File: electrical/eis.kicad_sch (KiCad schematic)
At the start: 57 parts

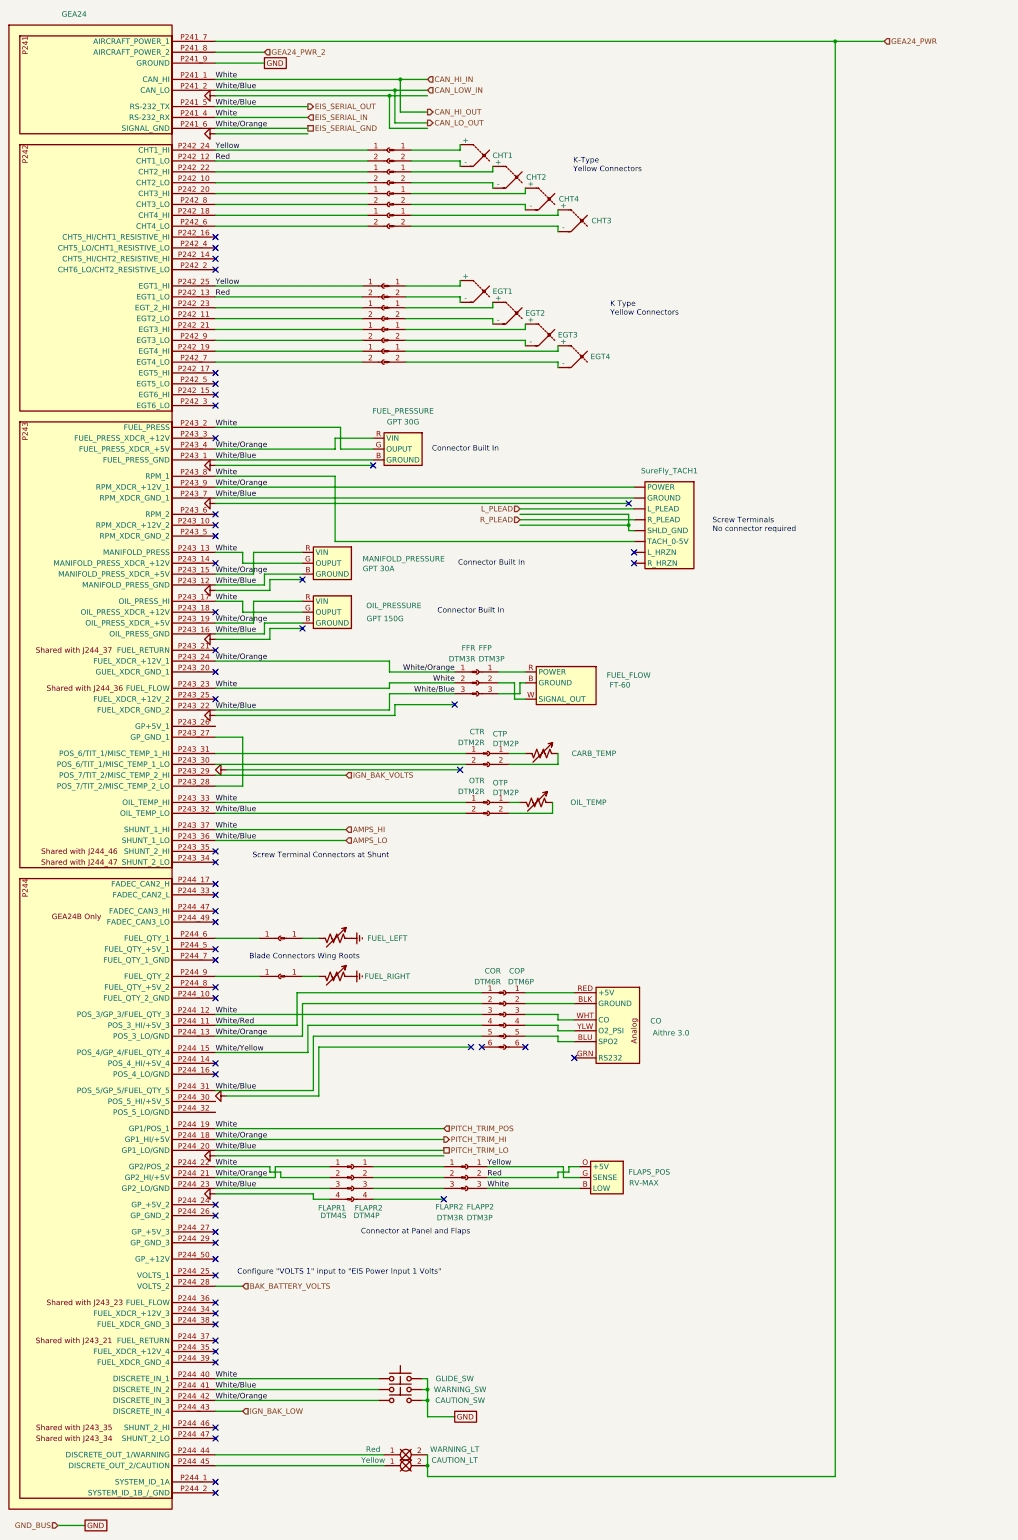
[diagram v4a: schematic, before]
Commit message: Assumed engine connector is sufficient for wiring on bench..
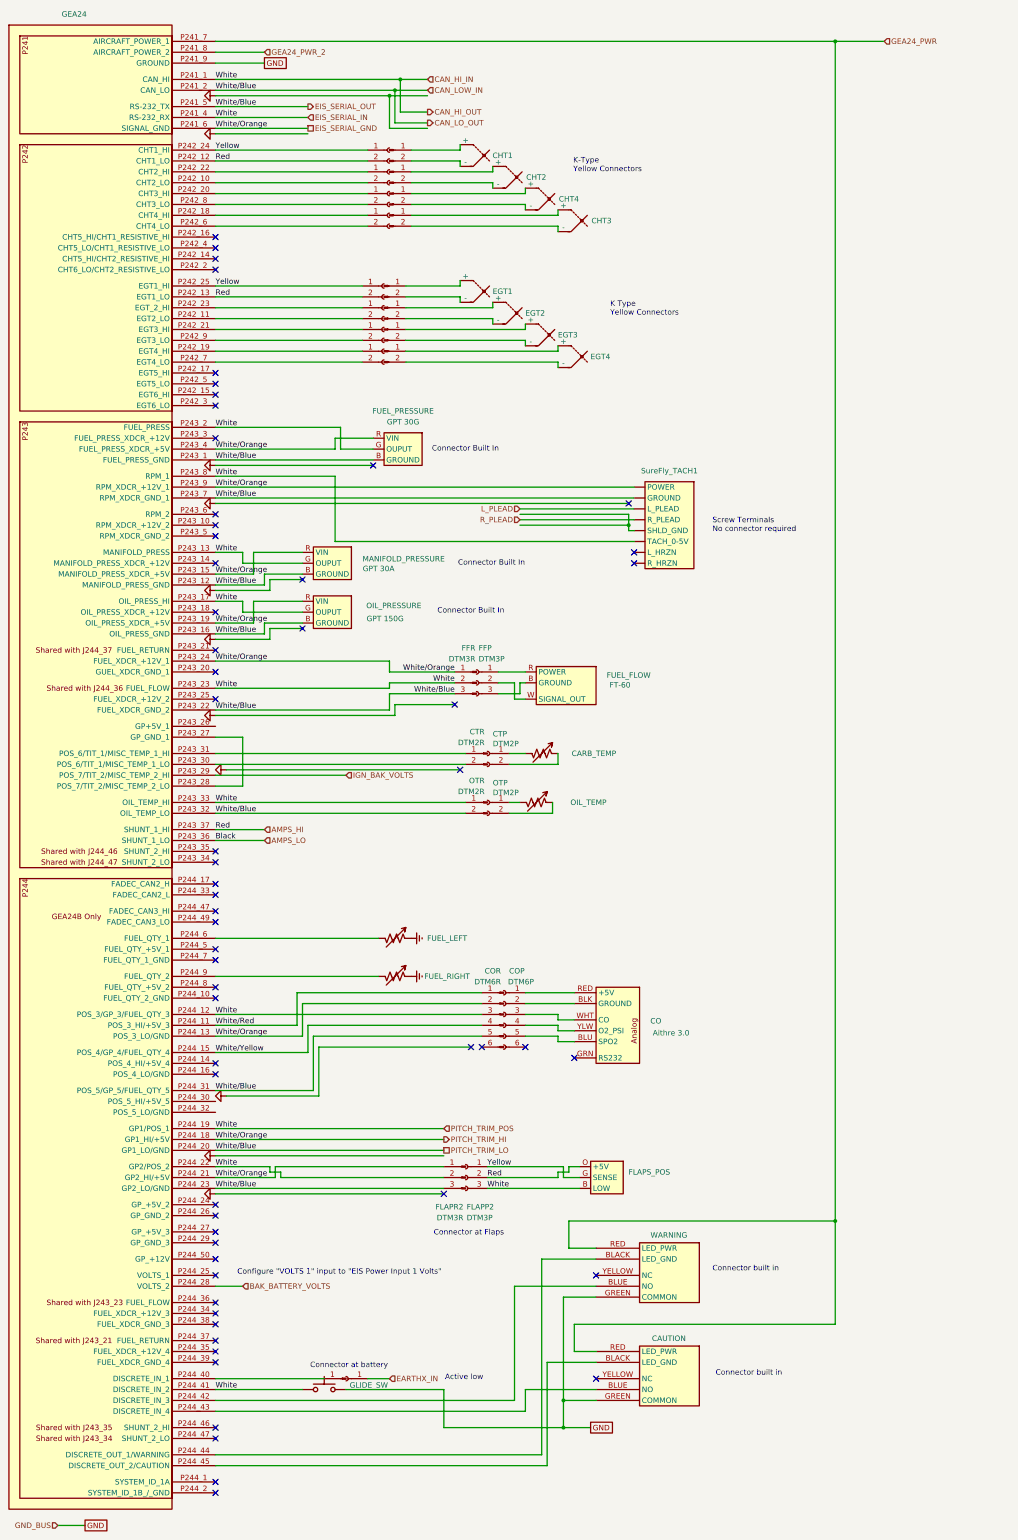
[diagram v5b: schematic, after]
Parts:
- removed CAUTION_LT: Yellow, symbol FlyerX:Bulb
- removed CAUTION_SW, WARNING_SW: SW_Push, symbol Switch:SW_Push
- removed FLAPR1: DTM4S, symbol Connector:Conn_01x04_Pin
- removed FLAPR2: DTM4P, symbol Connector:Conn_01x04_Socket
- removed LFP, RFP: Conn_01x01_Pin, symbol Connector:Conn_01x01_Pin
- removed LFR, RFR: Conn_01x01_Socket, symbol Connector:Conn_01x01_Socket
- removed WARNING_LT: Red, symbol FlyerX:Bulb
- added CAUTION, WARNING: ~, symbol flyerx:Apiele_Momentary_Illuminated_Button
- added EARTHXP: Conn_01x01_Pin, symbol Connector:Conn_01x01_Pin
- added EARTHXS: Conn_01x01_Socket, symbol Connector:Conn_01x01_Socket
- FLAPS_POS: value RV-MAX -> ~
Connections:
- net Red is gone; now on net AMPS_HI: CHT1R.2 (Pin_2), EGT1R.2 (Pin_2), FLAPP2.2 (Pin_2), FLAPS_POS.O (+5V), GEA24.P242_12 (CHT1_LO), GEA24.P242_13 (EGT1_LO)
- net AMPS_HI: no longer COR.3 (Pin_3), FFR.2 (Pin_2), FLAPP2.3 (Pin_3), FLAPS_POS.B (LOW), FUEL_PRESSURE.G (OUPUT), GEA24.P241_1 (CAN_HI), GEA24.P241_4 (RS-232_RX), GEA24.P243_13 (MANIFOLD_PRESS), GEA24.P243_17 (OIL_PRESS_HI), GEA24.P243_2 (FUEL_PRESS), GEA24.P243_23 (FUEL_FLOW), GEA24.P243_33 (OIL_TEMP_HI), GEA24.P243_8 (RPM_1), GEA24.P244_12 (POS_3/GP_3/FUEL_QTY_3), GEA24.P244_19 (GP1/POS_1), GEA24.P244_22 (GP2/POS_2), GEA24.P244_40 (DISCRETE_IN_1), GLIDE_SW.1, MANIFOLD_PRESSURE.G (OUPUT), OIL_PRESSURE.G (OUPUT), OTR.1 (Pin_1), SureFly_TACH1. (R_HRZN)
- net AMPS_LO: no longer COR.5 (Pin_5), FFR.3 (Pin_3), FUEL_PRESSURE.B (GROUND), GEA24.P241_2 (CAN_LO), GEA24.P241_5 (RS-232_TX), GEA24.P243_1 (FUEL_PRESS_GND), GEA24.P243_12 (MANIFOLD_PRESS_GND), GEA24.P243_16 (OIL_PRESS_GND), GEA24.P243_22 (FUEL_XDCR_GND_2), GEA24.P243_32 (OIL_TEMP_LO), GEA24.P243_7 (RPM_XDCR_GND_1), GEA24.P244_20 (GP1_LO/GND), GEA24.P244_23 (GP2_LO/GND), GEA24.P244_31 (POS_5/GP_5/FUEL_QTY_5), GEA24.P244_41 (DISCRETE_IN_2), MANIFOLD_PRESSURE.B (GROUND), OIL_PRESSURE.B (GROUND), OTR.2 (Pin_2), SureFly_TACH1. (R_HRZN)
- net EIS_SERIAL_GND: now also FLAPR2.1 (Pin_1); no longer GEA24.P244_42 (DISCRETE_IN_3)
- net GEA24_PWR: now also CAUTION.RED (LED_PWR), WARNING.RED (LED_PWR)
- net GND: now also CAUTION.GREEN (COMMON), WARNING.GREEN (COMMON)
- net at GEA24.P244_6 (FUEL_QTY_1): now also FUEL_LEFT.2
- net CAN_HI_IN: now reaches FLAPR2.2 (Pin_2)
- net CAN_HI_IN: now also COR.3 (Pin_3), FFR.2 (Pin_2), FLAPP2.3 (Pin_3), FLAPS_POS.B (LOW), FUEL_PRESSURE.G (OUPUT), GEA24.P241_1 (CAN_HI), GEA24.P241_4 (RS-232_RX), GEA24.P243_13 (MANIFOLD_PRESS), GEA24.P243_17 (OIL_PRESS_HI), GEA24.P243_2 (FUEL_PRESS), GEA24.P243_23 (FUEL_FLOW), GEA24.P243_33 (OIL_TEMP_HI), GEA24.P243_8 (RPM_1), GEA24.P244_12 (POS_3/GP_3/FUEL_QTY_3), GEA24.P244_19 (GP1/POS_1), GEA24.P244_22 (GP2/POS_2), GEA24.P244_41 (DISCRETE_IN_2), GLIDE_SW.1, MANIFOLD_PRESSURE.G (OUPUT), OIL_PRESSURE.G (OUPUT), OTR.1 (Pin_1), SureFly_TACH1. (R_HRZN)
- net CAN_LOW_IN: now reaches FLAPR2.3 (Pin_3)
- net CAN_LOW_IN: now also COR.5 (Pin_5), FFR.3 (Pin_3), FUEL_PRESSURE.B (GROUND), GEA24.P241_2 (CAN_LO), GEA24.P241_5 (RS-232_TX), GEA24.P243_1 (FUEL_PRESS_GND), GEA24.P243_12 (MANIFOLD_PRESS_GND), GEA24.P243_16 (OIL_PRESS_GND), GEA24.P243_22 (FUEL_XDCR_GND_2), GEA24.P243_32 (OIL_TEMP_LO), GEA24.P243_7 (RPM_XDCR_GND_1), GEA24.P244_20 (GP1_LO/GND), GEA24.P244_23 (GP2_LO/GND), GEA24.P244_31 (POS_5/GP_5/FUEL_QTY_5), MANIFOLD_PRESSURE.B (GROUND), OIL_PRESSURE.B (GROUND), OTR.2 (Pin_2), SureFly_TACH1. (R_HRZN)
- net at GEA24.P244_44 (DISCRETE_OUT_1/WARNING): now also WARNING.BLACK (LED_GND)
- net at GEA24.P244_45 (DISCRETE_OUT_2/CAUTION): now also CAUTION.BLACK (LED_GND)
- net at GEA24.P244_9 (FUEL_QTY_2): now also FUEL_RIGHT.2
- net IGN_BAK_LOW: no longer names the net of GEA24.P244_43 (DISCRETE_IN_4)
- net IGN_BAK_LOW: now also CAUTION.BLUE (NO)
- new net: EARTHXP.1 (Pin_1), GEA24.P244_40 (DISCRETE_IN_1)
- new net: GEA24.P244_42 (DISCRETE_IN_3), WARNING.BLUE (NO)
- new net EARTHX_IN: EARTHXS.1 (Pin_1)
- no-connect marks 58 -> 60
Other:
- note added: "Active low"
- note added: "Connector at Flaps"
- note added: "Connector at battery"
- note added: "Connector built in"
- note removed: "Blade Connectors Wing Roots"
- note removed: "Connector at Panel and Flaps"
- note removed: "Screw Terminal Connectors at Shunt"
- moved on the sheet: FUEL_LEFT, FUEL_RIGHT, GLIDE_SW

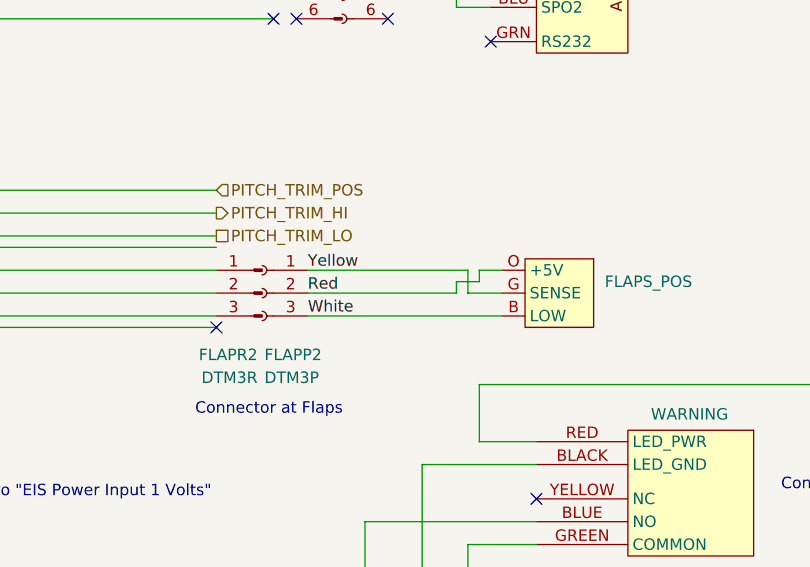
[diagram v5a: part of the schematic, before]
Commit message: Made flaps position sensor match colors of POS-12.
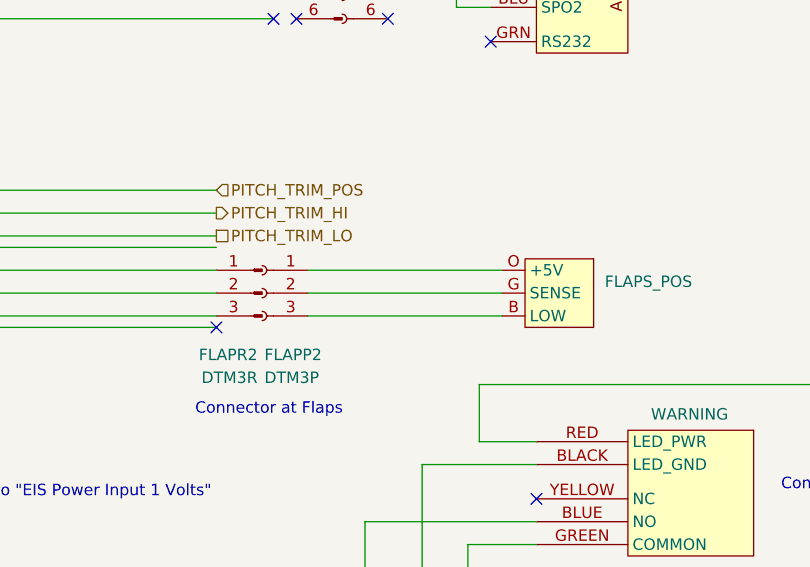
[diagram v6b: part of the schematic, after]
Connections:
- net AMPS_HI: no longer FLAPP2.2 (Pin_2), FLAPS_POS.O (+5V)
- net CAN_HI_IN: no longer FLAPP2.3 (Pin_3), FLAPS_POS.B (LOW)
- net Yellow: no longer FLAPP2.1 (Pin_1), FLAPS_POS.G (SENSE)
- new net: FLAPP2.1 (Pin_1), FLAPS_POS.O (+5V)
- new net: FLAPP2.2 (Pin_2), FLAPS_POS.G (SENSE)
- new net: FLAPP2.3 (Pin_3), FLAPS_POS.B (LOW)
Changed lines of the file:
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@@
 	(title_block
 		(title "EIS")
-		(date "2026-01-03")
-		(rev "1.2.4")
+		(date "2026-01-05")
+		(rev "1.2.5")
 		(company "N877RV")
 	)
@@
 	(wire
 		(pts
-			(xy 148.59 287.02) (xy 152.4 287.02)
-		)
-		(stroke
-			(width 0)
-			(type default)
-		)
-	)
-	(wire
-		(pts
 			(xy 86.36 243.84) (xy 129.54 243.84)
 		)
@@
 	(wire
 		(pts
-			(xy 148.59 284.48) (xy 148.59 287.02)
-		)
-		(stroke
-			(width 0)
-			(type default)
-		)
-	)
-	(wire
-		(pts
 			(xy 109.22 33.02) (xy 116.84 33.02)
 		)
@@
 	(wire
 		(pts
-			(xy 147.32 285.75) (xy 149.86 285.75)
-		)
-		(stroke
-			(width 0)
-			(type default)
-		)
-	)
-	(wire
-		(pts
 			(xy 67.31 193.04) (xy 97.79 193.04)
 		)
@@
 	(wire
 		(pts
-			(xy 130.81 284.48) (xy 148.59 284.48)
+			(xy 130.81 284.48) (xy 152.4 284.48)
 		)
 		(stroke
@@
 	(wire
 		(pts
-			(xy 147.32 287.02) (xy 147.32 285.75)
-		)
-		(stroke
-			(width 0)
-			(type default)
-		)
-	)
-	(wire
-		(pts
 			(xy 67.31 59.69) (xy 102.87 59.69)
 		)
@@
 	(wire
 		(pts
-			(xy 149.86 284.48) (xy 152.4 284.48)
-		)
-		(stroke
-			(width 0)
-			(type default)
-		)
-	)
-	(wire
-		(pts
 			(xy 139.7 341.63) (xy 139.7 336.55)
 		)
@@
 	(wire
 		(pts
-			(xy 130.81 287.02) (xy 147.32 287.02)
+			(xy 130.81 287.02) (xy 152.4 287.02)
 		)
 		(stroke
@@
 		(pts
 			(xy 67.31 26.67) (xy 78.74 26.67)
-		)
-		(stroke
-			(width 0)
-			(type default)
-		)
-	)
-	(wire
-		(pts
-			(xy 149.86 285.75) (xy 149.86 284.48)
 		)
 		(stroke
@@
 		)
 	)
-	(label "Red"
-		(at 130.81 287.02 0)
-		(effects
-			(font
-				(size 1.27 1.27)
-			)
-			(justify left bottom)
-		)
-	)
 	(label "White{slash}Blue"
 		(at 67.31 36.83 0)
@@
 		)
 	)
-	(label "White"
-		(at 130.81 289.56 0)
-		(effects
-			(font
-				(size 1.27 1.27)
-			)
-			(justify left bottom)
-		)
-	)
 	(label "White{slash}Orange"
 		(at 67.31 166.37 0)
@@
 		(effects
 			(font
-				(size 1.27 1.27)
-			)
-			(justify left bottom)
-		)
-	)
-	(label "Yellow"
-		(at 130.81 284.48 0)
-		(effects
-			(font

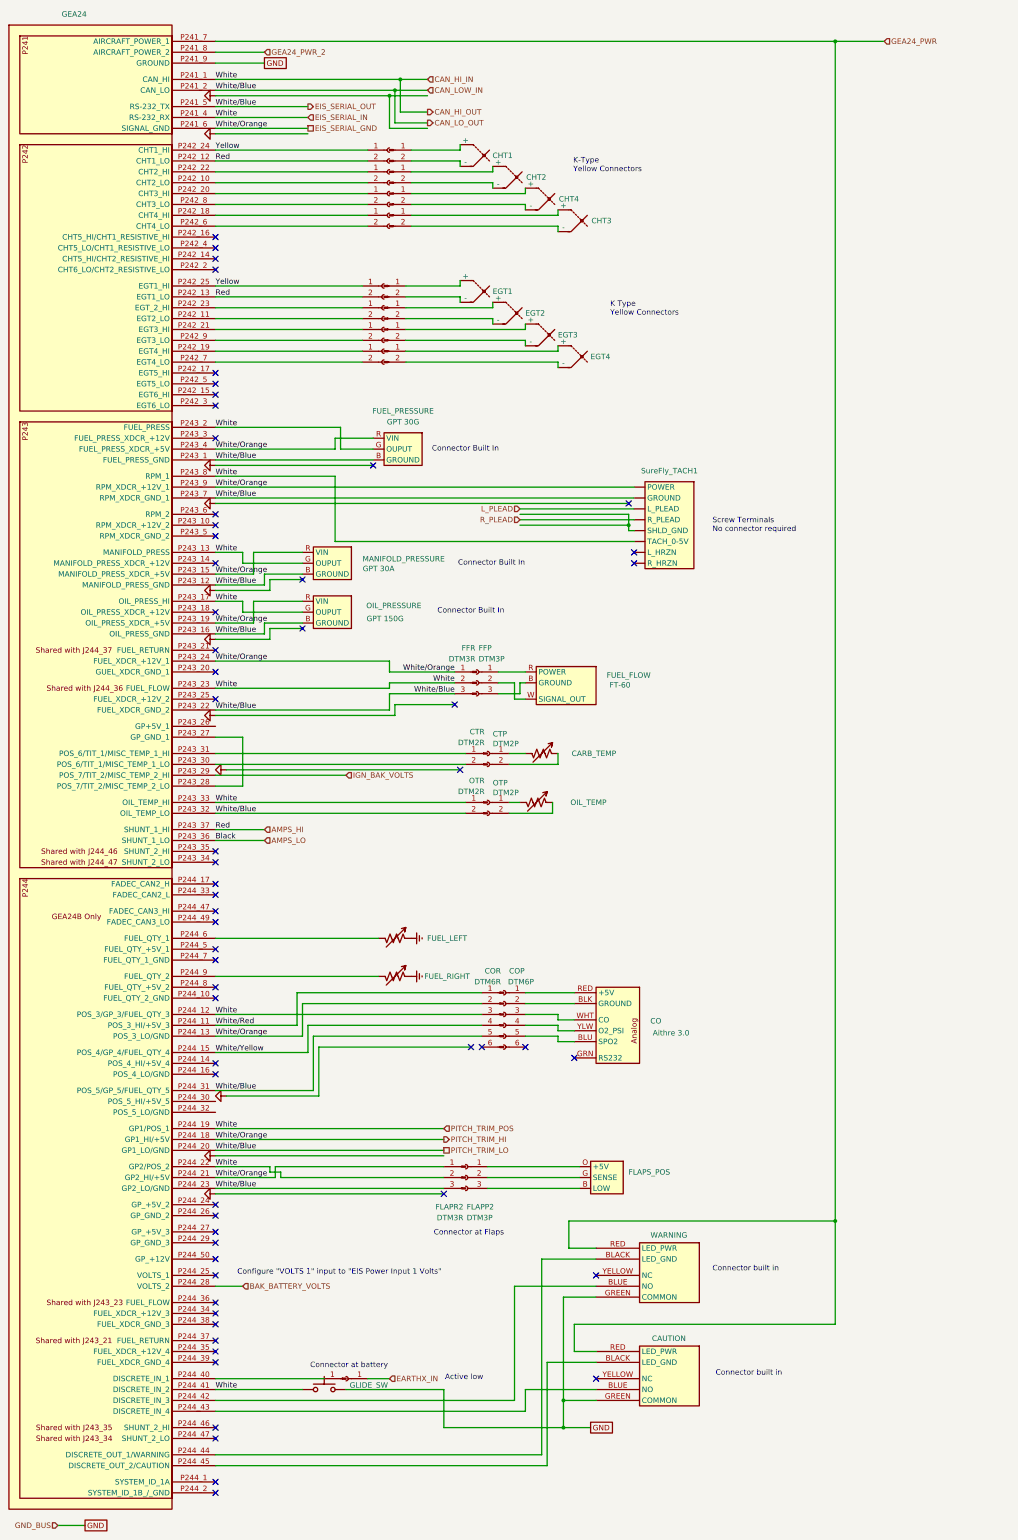
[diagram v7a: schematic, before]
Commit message: Added connector for discrete buttons on EIS.
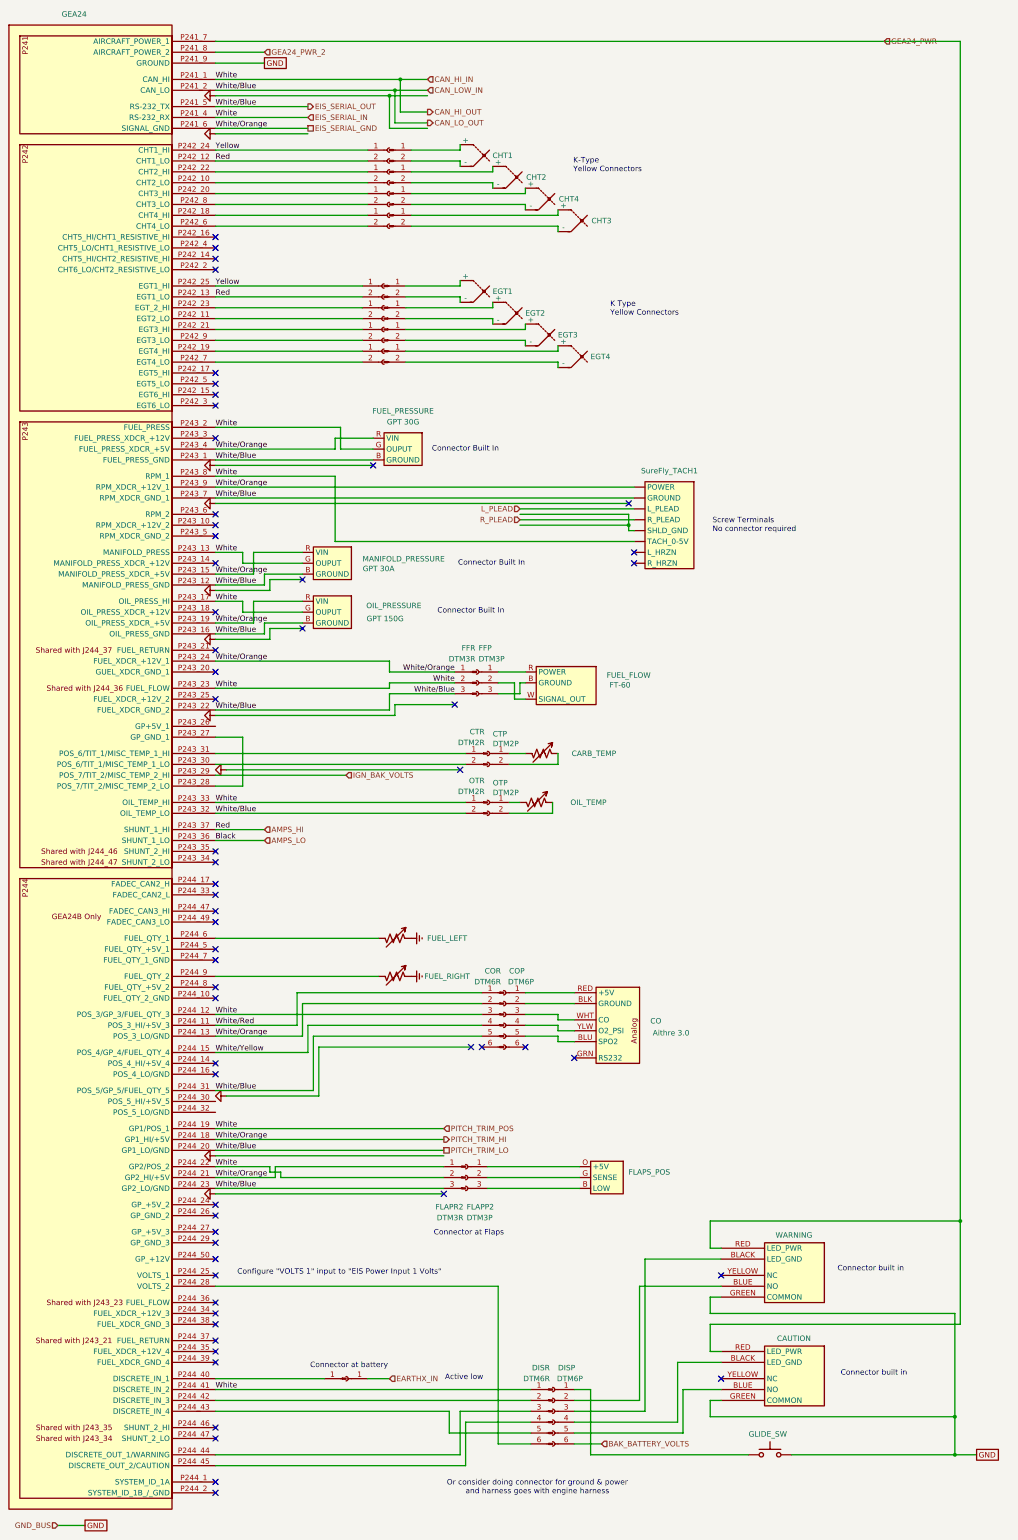
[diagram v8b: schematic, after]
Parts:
- added DISP: DTM6P, symbol Connector:Conn_01x06_Socket
- added DISR: DTM6R, symbol Connector:Conn_01x06_Pin
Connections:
- net BAK_BATTERY_VOLTS: now also DISP.6 (Pin_6); no longer GEA24.P244_28 (VOLTS_2)
- net CAN_HI_IN: now also DISR.1 (Pin_1); no longer GLIDE_SW.1
- net at WARNING.BLUE (NO): now also DISP.2 (Pin_2); no longer GEA24.P244_42 (DISCRETE_IN_3)
- net at CAUTION.BLUE (NO): now also DISP.5 (Pin_5); no longer GEA24.P244_43 (DISCRETE_IN_4)
- net at WARNING.BLACK (LED_GND): now also DISP.3 (Pin_3); no longer GEA24.P244_44 (DISCRETE_OUT_1/WARNING)
- net at CAUTION.BLACK (LED_GND): now also DISP.4 (Pin_4); no longer GEA24.P244_45 (DISCRETE_OUT_2/CAUTION)
- new net: DISP.1 (Pin_1), GLIDE_SW.1
- new net: DISR.6 (Pin_6), GEA24.P244_28 (VOLTS_2)
- new net: DISR.2 (Pin_2), GEA24.P244_42 (DISCRETE_IN_3)
- new net: DISR.5 (Pin_5), GEA24.P244_43 (DISCRETE_IN_4)
- new net: DISR.3 (Pin_3), GEA24.P244_44 (DISCRETE_OUT_1/WARNING)
- new net: DISR.4 (Pin_4), GEA24.P244_45 (DISCRETE_OUT_2/CAUTION)
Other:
- note added: "Or consider doing connector for ground & power and harness goes with engine harness"
- moved on the sheet: CAUTION, GLIDE_SW, WARNING
